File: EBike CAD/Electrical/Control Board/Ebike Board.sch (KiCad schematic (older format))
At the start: 0 parts

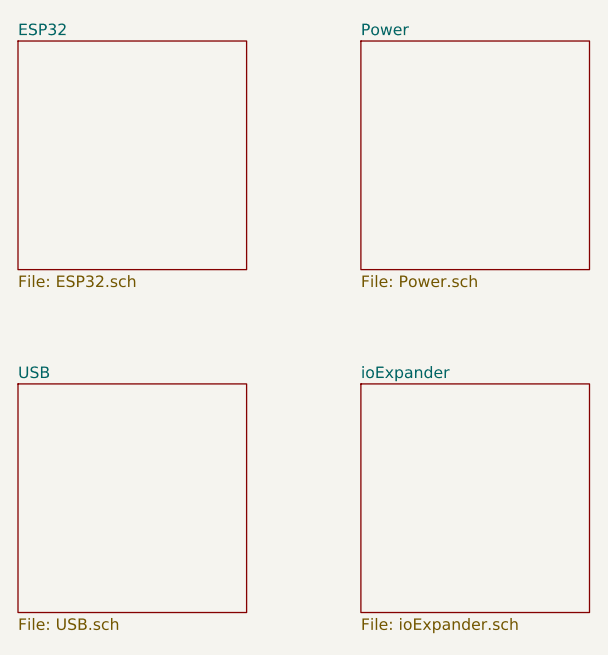
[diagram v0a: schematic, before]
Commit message: -Software ported to new ESP32 board -Added OTA updates -Added bluetooth serial debug -Added IOexpander -Added headlight functionality
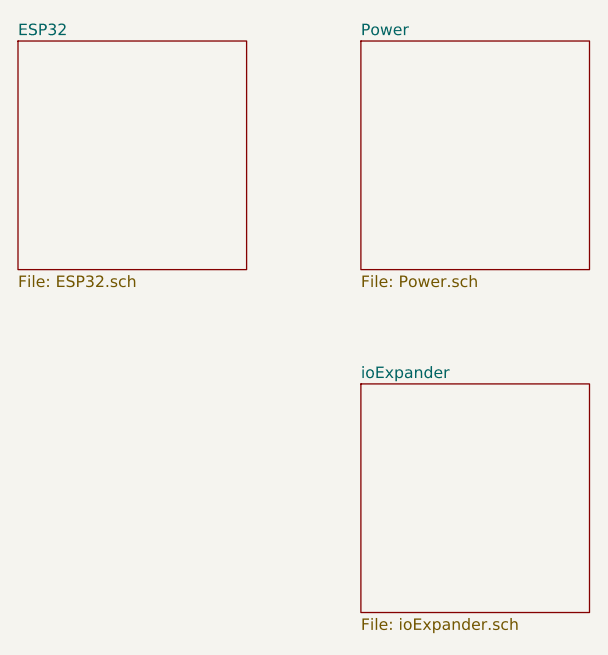
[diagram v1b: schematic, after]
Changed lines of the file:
@@
 $Descr A4 11693 8268
 encoding utf-8
-Sheet 1 5
+Sheet 1 4
 Title ""
 Date ""
@@
 $EndSheet
 $Sheet
-S 1500 2500 1000 1000
-U 5E5F97D9
-F0 "USB" 50
-F1 "USB.sch" 50
-$EndSheet
-$Sheet
